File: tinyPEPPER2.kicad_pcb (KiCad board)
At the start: 4 copper layers, 20 x 20 mm, 163 parts, among them T1 BC847, T10 BC847, T11 BC847, T12 BC847, T2 BC847, T3 BC847, T4 BC847, T5 BC847, T6 BC847, T7 BC847, T8 BC847, T9 BC847, U1 AP131-30, U2 EFM8BB10, U3 EFM8BB10, U4 EFM8BB10, U5 EFM8BB10

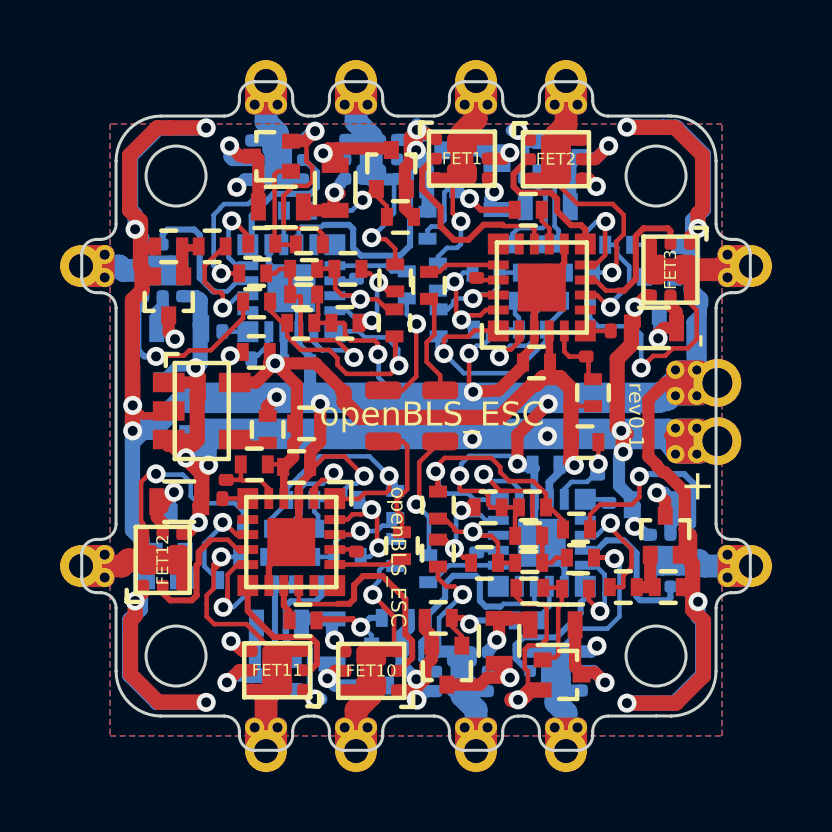
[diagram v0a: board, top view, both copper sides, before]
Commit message: Revert tinyPEPPER2.kicad_pcb to pre-sync state, restoring 299 orphaned nets
Update PCB from Schematic (run after resetting schematic annotation)
blanked the net assignment on 299 existing track/via objects, causing
32 unconnected items and 135 shorting items in DRC. Reverting the PCB
to commit 1207ddc (last known-good state, same footprint/track/via
count, same branding and 3D model paths) restores full connectivity.
Silkscreen reference numbers revert to the pre-reannotation scheme
(U201 etc instead of U2) as a cosmetic tradeoff; schematic is unaffected.

Co-Authored-By: Claude Sonnet 5 <noreply@anthropic.com>
Claude-Session: https://claude.ai/code/session_01FXVgZdFwN8FRfUqtWPU5iZ
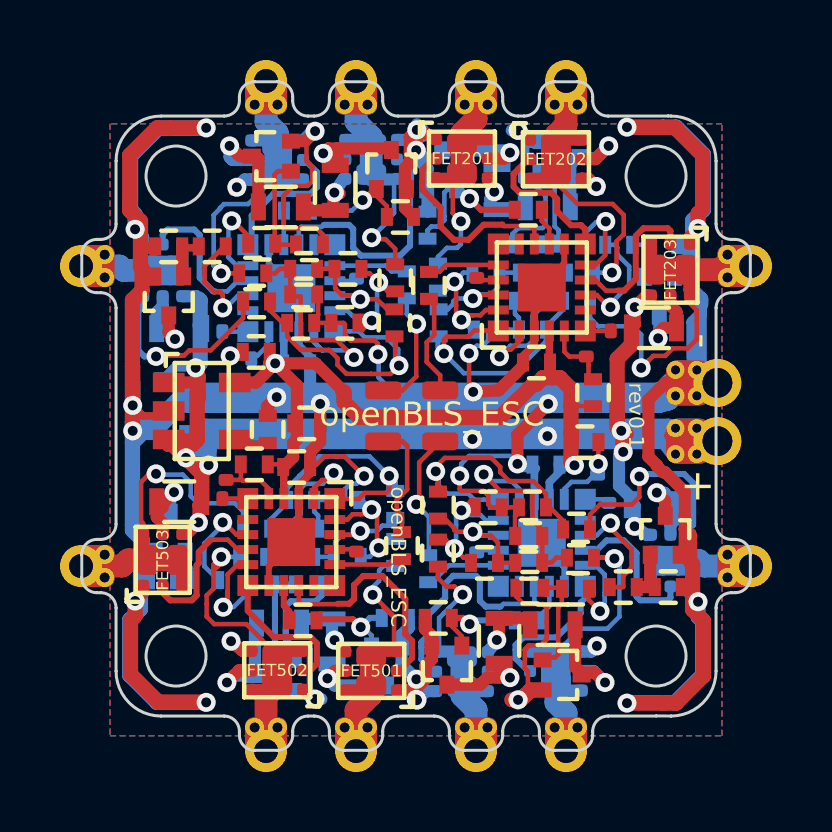
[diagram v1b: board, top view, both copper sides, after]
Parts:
- renumbered BL_TX1 to BL_TX201, BL_TX2 to BL_TX301, BL_TX3 to BL_TX401, BL_TX4 to BL_TX501, C2 to C1000, C4 to C1001, C1 to C1002, C3 to C1003, C5 to C201, C6 to C202, C7 to C203, C8 to C204, C9 to C301, C10 to C302, C11 to C303, C12 to C304, C13 to C401, C14 to C402, C15 to C403, C16 to C404, C17 to C501, C18 to C502, C19 to C503, C20 to C504, FET1 to FET201, FET2 to FET202, FET3 to FET203, FET4 to FET301, FET5 to FET302, FET6 to FET303, FET7 to FET401, FET8 to FET402, FET9 to FET403, FET10 to FET501, FET11 to FET502, FET12 to FET503, OUT_A1 to OUT_A201, OUT_A2 to OUT_A301, OUT_A3 to OUT_A401, OUT_A4 to OUT_A501, OUT_B1 to OUT_B201, OUT_B2 to OUT_B301, OUT_B3 to OUT_B401, OUT_B4 to OUT_B501, OUT_C1 to OUT_C201, OUT_C2 to OUT_C301, OUT_C3 to OUT_C401, OUT_C4 to OUT_C501, R1 to R201, R12 to R202, R13 to R203, R14 to R204, R15 to R205, R16 to R206, R17 to R207, R18 to R208, R19 to R209, R20 to R210, R3 to R211, R4 to R212, R5 to R213, R11 to R214, R6 to R215, R7 to R216, R8 to R217, R9 to R218, R10 to R219, R2 to R220, R21 to R301, R32 to R302, R33 to R303, R34 to R304, R35 to R305, R36 to R306, R37 to R307, R38 to R308, R39 to R309, R40 to R310, R23 to R311, R24 to R312, R25 to R313, R31 to R314, R26 to R315, R27 to R316, R28 to R317, R29 to R318, R30 to R319, R22 to R320, R41 to R401, R52 to R402, R53 to R403, R54 to R404, R55 to R405, R56 to R406, R57 to R407, R58 to R408, R59 to R409, R60 to R410, R43 to R411, R44 to R412, R45 to R413, R51 to R414, R46 to R415, R47 to R416, R48 to R417, R49 to R418, R50 to R419, R42 to R420, R61 to R501, R72 to R502, R73 to R503, R74 to R504, R75 to R505, R76 to R506, R77 to R507, R78 to R508, R79 to R509, R80 to R510, R63 to R511, R64 to R512, R65 to R513, R71 to R514, R66 to R515, R67 to R516, R68 to R517, R69 to R518, R70 to R519, R62 to R520, T1 to T201, T2 to T202, T3 to T203, T4 to T301, T5 to T302, T6 to T303, T7 to T401, T8 to T402, T9 to T403, T10 to T501, T11 to T502, T12 to T503, TP1 to TP10, TP3 to TP103, TP4 to TP104, TP5 to TP105, TP6 to TP106, TP2 to TP12, TP8 to TP202, TP7 to TP203, TP10 to TP302, TP9 to TP303, TP12 to TP402, TP11 to TP403, TP14 to TP502, TP13 to TP503, U2 to U201, U3 to U301, U4 to U401, U5 to U501
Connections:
- net /single esc 3/RC_IN_0 renamed /single esc 3/RC_IN
- net /single esc 4/RC_IN_0 renamed /single esc 4/RC_IN
- R202 pad 1: Net-(R12-~-Pad1) -> Net-(R202-Pad1)
- R202 pad 2: Net-(R12-~-Pad2) -> Net-(R202-Pad2)
- R203 pad 1: Net-(R12-~-Pad2) -> Net-(R202-Pad2)
- R204 pad 1: Net-(U2-P0.3) -> Net-(R202-Pad1)
- R204 pad 2: Net-(R14-~-Pad2) -> Net-(R204-Pad2)
- R205 pad 1: Net-(R14-~-Pad2) -> Net-(R204-Pad2)
- R206 pad 1: Net-(R12-~-Pad1) -> Net-(R202-Pad1)
- R206 pad 2: Net-(R16-~-Pad2) -> Net-(R206-Pad2)
- R207 pad 1: Net-(R16-~-Pad2) -> Net-(R206-Pad2)
- R208 pad 2: Net-(U2-P0.2) -> Net-(R202-Pad2)
- R209 pad 2: Net-(U2-P0.0) -> Net-(R204-Pad2)
- R210 pad 2: Net-(U2-P0.1) -> Net-(R206-Pad2)
- R302 pad 1: Net-(R32-~-Pad1) -> Net-(R302-Pad1)
- R302 pad 2: Net-(R32-~-Pad2) -> Net-(R302-Pad2)
- R303 pad 1: Net-(R32-~-Pad2) -> Net-(R302-Pad2)
- R304 pad 1: Net-(U3-P0.3) -> Net-(R302-Pad1)
- R304 pad 2: Net-(R34-~-Pad2) -> Net-(R304-Pad2)
- R305 pad 1: Net-(R34-~-Pad2) -> Net-(R304-Pad2)
- R306 pad 1: Net-(R32-~-Pad1) -> Net-(R302-Pad1)
- R306 pad 2: Net-(R36-~-Pad2) -> Net-(R306-Pad2)
- R307 pad 1: Net-(R36-~-Pad2) -> Net-(R306-Pad2)
- R308 pad 2: Net-(U3-P0.2) -> Net-(R302-Pad2)
- R309 pad 2: Net-(U3-P0.0) -> Net-(R304-Pad2)
- R310 pad 2: Net-(U3-P0.1) -> Net-(R306-Pad2)
- R402 pad 1: Net-(R52-~-Pad1) -> Net-(R402-Pad1)
- R402 pad 2: Net-(R52-~-Pad2) -> Net-(R402-Pad2)
- R403 pad 1: Net-(R52-~-Pad2) -> Net-(R402-Pad2)
- R404 pad 1: Net-(U4-P0.3) -> Net-(R402-Pad1)
- R404 pad 2: Net-(R54-~-Pad2) -> Net-(R404-Pad2)
- R405 pad 1: Net-(R54-~-Pad2) -> Net-(R404-Pad2)
- R406 pad 1: Net-(R52-~-Pad1) -> Net-(R402-Pad1)
- R406 pad 2: Net-(R56-~-Pad2) -> Net-(R406-Pad2)
- R407 pad 1: Net-(R56-~-Pad2) -> Net-(R406-Pad2)
- R408 pad 2: Net-(U4-P0.2) -> Net-(R402-Pad2)
- R409 pad 2: Net-(U4-P0.0) -> Net-(R404-Pad2)
- R410 pad 2: Net-(U4-P0.1) -> Net-(R406-Pad2)
- R502 pad 1: Net-(R72-~-Pad1) -> Net-(R502-Pad1)
- R502 pad 2: Net-(R72-~-Pad2) -> Net-(R502-Pad2)
- R503 pad 1: Net-(R72-~-Pad2) -> Net-(R502-Pad2)
- R504 pad 1: Net-(U5-P0.3) -> Net-(R502-Pad1)
- R504 pad 2: Net-(R74-~-Pad2) -> Net-(R504-Pad2)
- R505 pad 1: Net-(R74-~-Pad2) -> Net-(R504-Pad2)
- R506 pad 1: Net-(R72-~-Pad1) -> Net-(R502-Pad1)
- R506 pad 2: Net-(R76-~-Pad2) -> Net-(R506-Pad2)
- R507 pad 1: Net-(R76-~-Pad2) -> Net-(R506-Pad2)
- R508 pad 2: Net-(U5-P0.2) -> Net-(R502-Pad2)
- R509 pad 2: Net-(U5-P0.0) -> Net-(R504-Pad2)
- R510 pad 2: Net-(U5-P0.1) -> Net-(R506-Pad2)
- U201 pad 1: Net-(U2-P0.1) -> Net-(R206-Pad2)
- U201 pad 15: unconnected-(U2-P0.7-Pad15) -> (no net)
- U201 pad 16: unconnected-(U2-P0.6-Pad16) -> (no net)
- U201 pad 19: Net-(U2-P0.3) -> Net-(R202-Pad1)
- U201 pad 2: Net-(U2-P0.0) -> Net-(R204-Pad2)
- U201 pad 20: Net-(U2-P0.2) -> Net-(R202-Pad2)
- U201 pad 7: unconnected-(U2-P1.6-Pad7) -> (no net)
- U301 pad 1: Net-(U3-P0.1) -> Net-(R306-Pad2)
- U301 pad 15: unconnected-(U3-P0.7-Pad15) -> (no net)
- U301 pad 16: unconnected-(U3-P0.6-Pad16) -> (no net)
- U301 pad 19: Net-(U3-P0.3) -> Net-(R302-Pad1)
- U301 pad 2: Net-(U3-P0.0) -> Net-(R304-Pad2)
- U301 pad 20: Net-(U3-P0.2) -> Net-(R302-Pad2)
- U301 pad 7: unconnected-(U3-P1.6-Pad7) -> (no net)
- U401 pad 1: Net-(U4-P0.1) -> Net-(R406-Pad2)
- U401 pad 15: unconnected-(U4-P0.7-Pad15) -> (no net)
- U401 pad 16: unconnected-(U4-P0.6-Pad16) -> (no net)
- U401 pad 19: Net-(U4-P0.3) -> Net-(R402-Pad1)
- U401 pad 2: Net-(U4-P0.0) -> Net-(R404-Pad2)
- U401 pad 20: Net-(U4-P0.2) -> Net-(R402-Pad2)
- U401 pad 7: unconnected-(U4-P1.6-Pad7) -> (no net)
- U501 pad 1: Net-(U5-P0.1) -> Net-(R506-Pad2)
- U501 pad 15: unconnected-(U5-P0.7-Pad15) -> (no net)
- U501 pad 16: unconnected-(U5-P0.6-Pad16) -> (no net)
- U501 pad 19: Net-(U5-P0.3) -> Net-(R502-Pad1)
- U501 pad 2: Net-(U5-P0.0) -> Net-(R504-Pad2)
- U501 pad 20: Net-(U5-P0.2) -> Net-(R502-Pad2)
- U501 pad 7: unconnected-(U5-P1.6-Pad7) -> (no net)
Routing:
- net (no net): track 104.2 -> 0.00 mm, vias 20 -> 0
- net Net-(R306-Pad2): track 0.00 -> 11.1 mm, vias 0 -> 1
- net Net-(R406-Pad2): track 0.00 -> 10.6 mm, vias 0 -> 1
- net Net-(R506-Pad2): track 0.00 -> 9.35 mm, vias 0 -> 1
- net Net-(R206-Pad2): track 0.00 -> 9.34 mm, vias 0 -> 1
- net Net-(R304-Pad2): track 0.00 -> 8.10 mm, vias 0 -> 1
- net Net-(R404-Pad2): track 0.00 -> 7.08 mm, vias 0 -> 1
- net Net-(R204-Pad2): track 0.00 -> 5.74 mm, vias 0 -> 1
- net Net-(R504-Pad2): track 0.00 -> 5.70 mm, vias 0 -> 1
- net Net-(R202-Pad1): track 0.00 -> 4.80 mm, vias 0 -> 1
- net Net-(R502-Pad1): track 0.00 -> 4.72 mm, vias 0 -> 1
- net Net-(R502-Pad2): track 0.00 -> 4.69 mm, vias 0 -> 2
- net Net-(R202-Pad2): track 0.00 -> 4.69 mm, vias 0 -> 2
- net Net-(R402-Pad2): track 0.00 -> 4.69 mm, vias 0 -> 2
- net Net-(R302-Pad1): track 0.00 -> 4.64 mm, vias 0 -> 1
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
